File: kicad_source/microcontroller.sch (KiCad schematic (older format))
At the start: 50 parts, among them CN1 MEM2061-01-188-00-A, CN2 FSH-105-04-L-DH-SL, CN5 CONN_01X14, CN6 CONN_01X04, SW1 TAST_VER, SW2 TAST_VER, SW3 434123043816, SW4 TAST_VER, U1 W25Q80D, U2 ATECC608A, U3 FE310-G002, U8 BMA253, Y1 FA-238 16.0000MB-C3

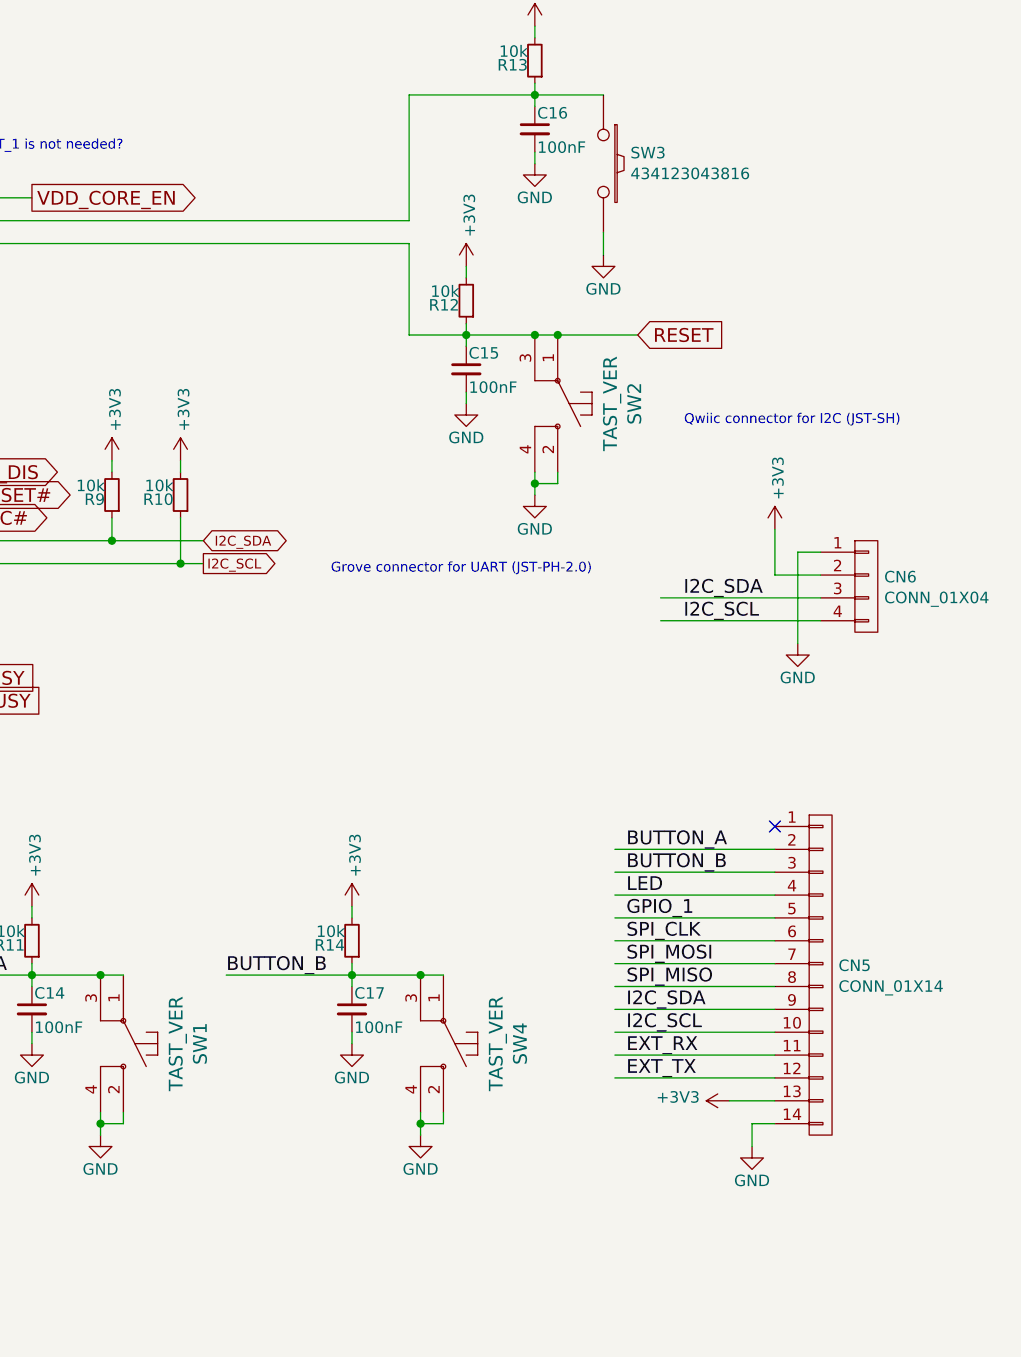
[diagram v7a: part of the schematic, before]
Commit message: optimized parts for BOM costs
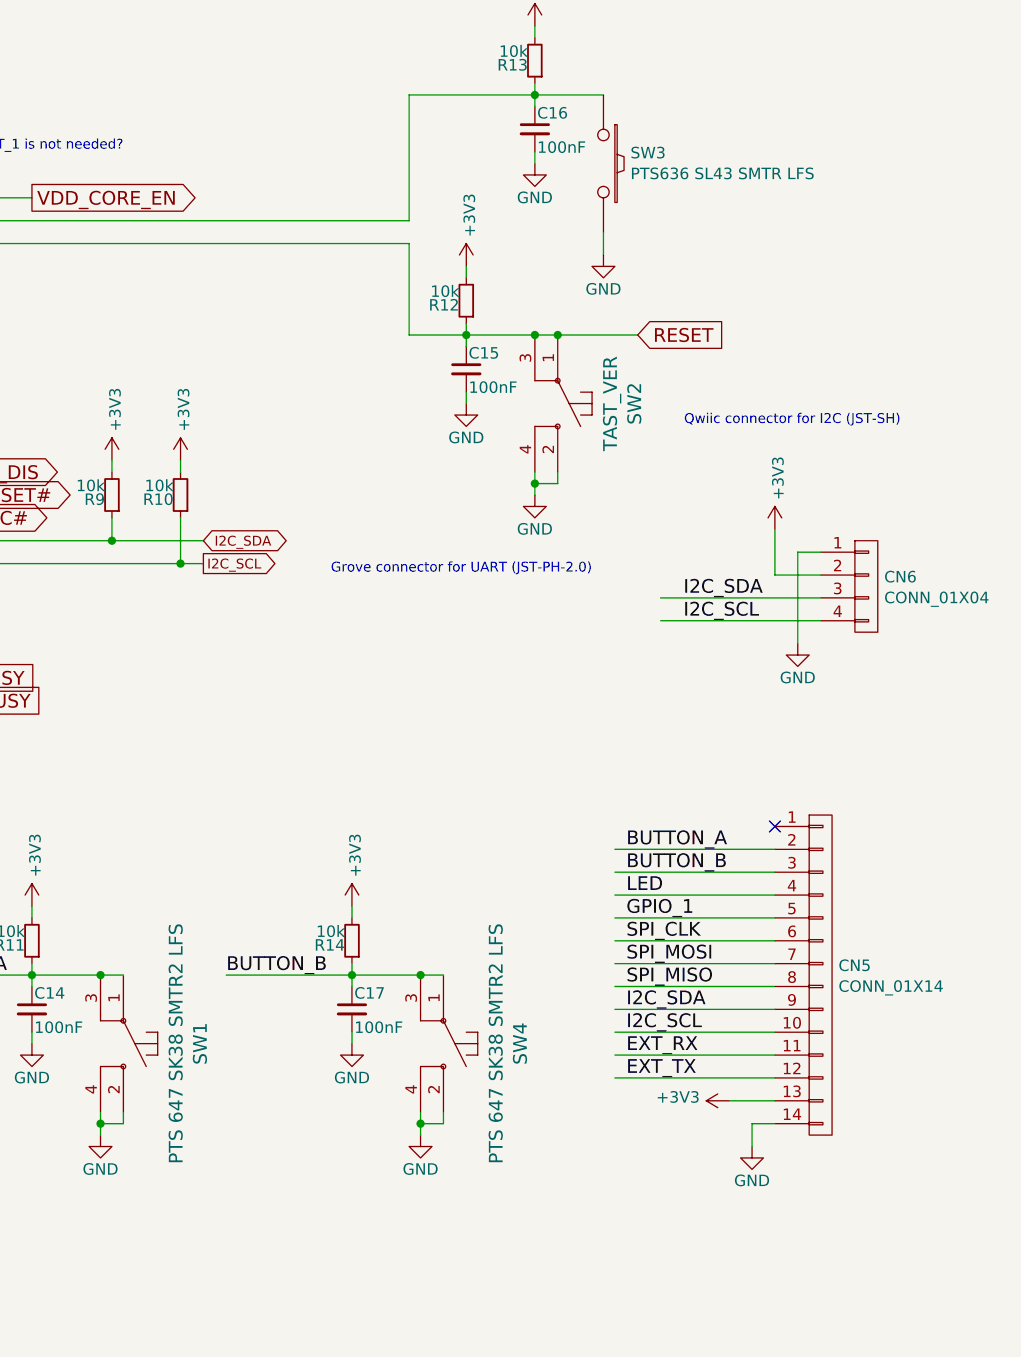
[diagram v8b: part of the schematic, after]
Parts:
- SW1, SW4: value TAST_VER -> PTS 647 SK38 SMTR2 LFS; footprint mechanical-switches:WE_430182050816 -> mechanical-switches:CK_PTS647
- SW3: value 434123043816 -> PTS636 SL43 SMTR LFS
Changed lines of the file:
@@
 P 7600 5800
 F 0 "SW1" H 7600 6137 60  0000 C CNN
-F 1 "TAST_VER" H 7600 6031 60  0000 C CNN
-F 2 "mechanical-switches:WE_430182050816" H 8450 5850 60  0001 C CNN
+F 1 "PTS 647 SK38 SMTR2 LFS" H 7600 6031 60  0000 C CNN
+F 2 "mechanical-switches:CK_PTS647" H 8450 5850 60  0001 C CNN
 F 3 "" H 8450 5850 60  0000 C CNN
 	1    7600 5800
@@
 P 9000 5800
 F 0 "SW4" H 9000 6137 60  0000 C CNN
-F 1 "TAST_VER" H 9000 6031 60  0000 C CNN
-F 2 "mechanical-switches:WE_430182050816" H 9850 5850 60  0001 C CNN
+F 1 "PTS 647 SK38 SMTR2 LFS" H 9000 6031 60  0000 C CNN
+F 2 "mechanical-switches:CK_PTS647" H 9850 5850 60  0001 C CNN
 F 3 "" H 9850 5850 60  0000 C CNN
 	1    9000 5800
@@
 P 9700 1950
 F 0 "SW3" V 9654 2068 50  0000 L CNN
-F 1 "434123043816" V 9745 2068 50  0000 L CNN
+F 1 "PTS636 SL43 SMTR LFS " V 9745 2068 50  0000 L CNN
 F 2 "mechanical-switches:smd_push" V 9791 2068 50  0001 L CNN
 F 3 "" H 9700 1950 50  0000 C CNN
